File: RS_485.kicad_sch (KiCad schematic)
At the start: 17 parts, among them IC1 SP3071EEN-L/TR

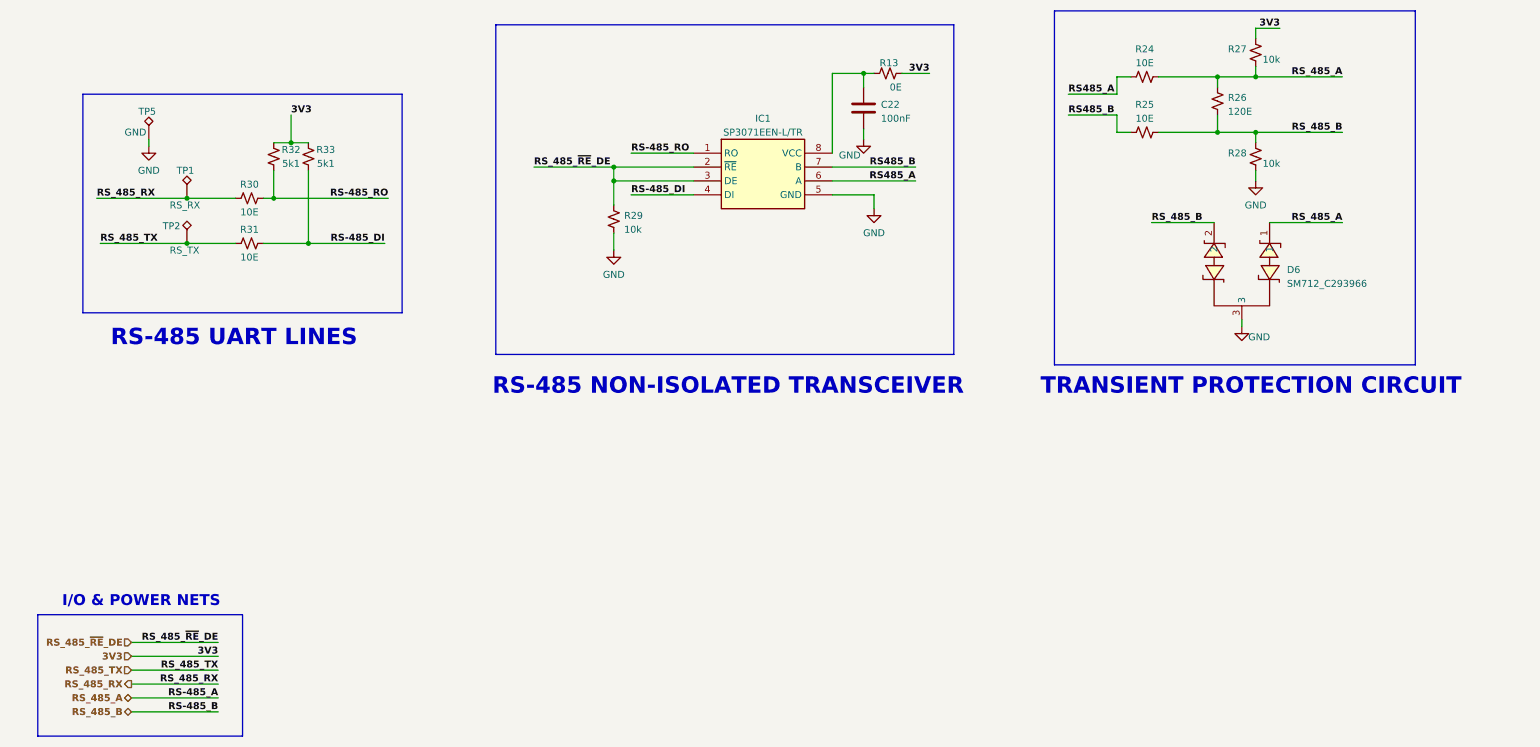
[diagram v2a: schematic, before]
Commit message: Arranged IP5306, Added support for USB-To-RS485
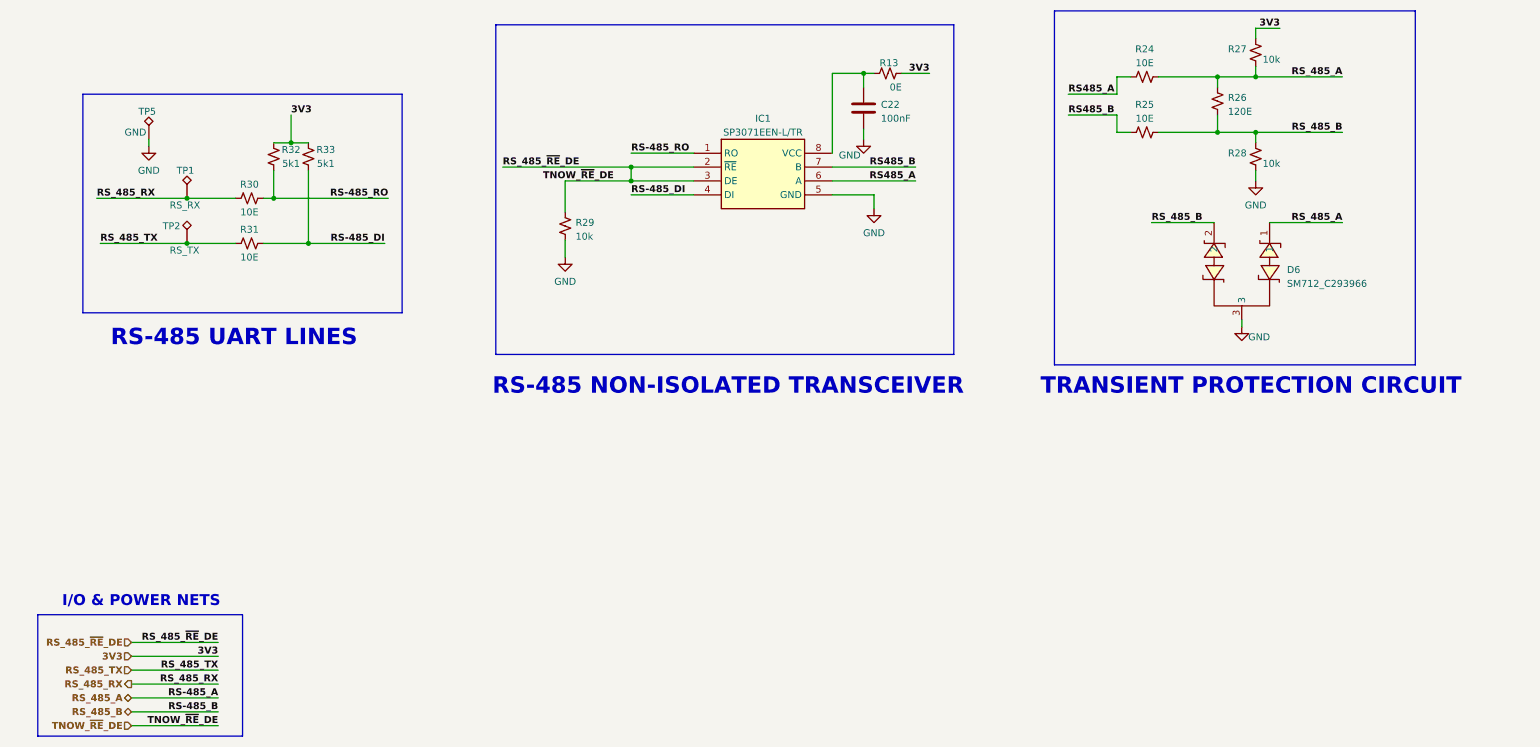
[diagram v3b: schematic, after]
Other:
- moved on the sheet: R29
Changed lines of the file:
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@@
   (junction (at 235.585 81.28) (diameter 0) (color 0 0 0 0)
   )
-  (junction (at 125.095 90.17) (diameter 0) (color 0 0 0 0)
+  (junction (at 128.27 87.63) (diameter 0) (color 0 0 0 0)
+  )
+  (junction (at 128.27 90.17) (diameter 0) (color 0 0 0 0)
   )
   (junction (at 46.99 101.6) (diameter 0) (color 0 0 0 0)
@@
   (junction (at 46.99 93.345) (diameter 0) (color 0 0 0 0)
   )
-  (junction (at 125.095 87.63) (diameter 0) (color 0 0 0 0)
-  )
   (junction (at 235.585 71.12) (diameter 0) (color 0 0 0 0)
   )
@@
     (stroke (width 0) (type default))
   )
-  (wire (pts (xy 125.095 94.615) (xy 125.095 90.17))
+  (wire (pts (xy 116.205 95.885) (xy 116.205 90.17))
     (stroke (width 0) (type default))
   )
@@
     (stroke (width 0) (type default))
   )
-  (wire (pts (xy 125.095 87.63) (xy 125.095 90.17))
+  (wire (pts (xy 128.27 87.63) (xy 128.27 90.17))
     (stroke (width 0) (type default))
   )
@@
     (stroke (width 1) (type default) (color 72 72 72 1))
   )
+  (wire (pts (xy 128.27 87.63) (xy 139.7 87.63))
+    (stroke (width 0) (type default))
+  )
   (wire (pts (xy 224.79 71.12) (xy 235.585 71.12))
     (stroke (width 0) (type default))
@@
     (stroke (width 0.5) (type default) (color 0 194 0 1))
   )
-  (wire (pts (xy 125.095 99.695) (xy 125.095 102.87))
-    (stroke (width 0) (type default))
-  )
   (wire (pts (xy 46.99 93.345) (xy 55.88 93.345))
     (stroke (width 0) (type default))
@@
     (stroke (width 0) (type default))
   )
+  (wire (pts (xy 104.775 87.63) (xy 128.27 87.63))
+    (stroke (width 0) (type default))
+  )
   (bus (pts (xy 103.505 61.595) (xy 103.505 121.92))
     (stroke (width 1) (type default) (color 72 72 72 1))
+  )
+  (wire (pts (xy 116.205 100.965) (xy 116.205 104.14))
+    (stroke (width 0) (type default))
+  )
+  (wire (pts (xy 52.705 189.865) (xy 36.83 189.865))
+    (stroke (width 0.5) (type default) (color 0 194 0 1))
   )
   (wire (pts (xy 62.865 88.265) (xy 62.865 93.345))
@@
     (stroke (width 1) (type default) (color 72 72 72 1))
   )
-  (wire (pts (xy 110.49 87.63) (xy 125.095 87.63))
-    (stroke (width 0) (type default))
-  )
-  (wire (pts (xy 125.095 90.17) (xy 139.7 90.17))
-    (stroke (width 0) (type default))
-  )
   (wire (pts (xy 240.03 116.84) (xy 240.03 115.57))
     (stroke (width 0) (type default))
@@
     (stroke (width 0.5) (type default) (color 255 0 0 1))
   )
-  (wire (pts (xy 125.095 87.63) (xy 139.7 87.63))
-    (stroke (width 0) (type default))
-  )
   (wire (pts (xy 128.27 85.09) (xy 139.7 85.09))
     (stroke (width 0) (type default))
@@
   )
   (wire (pts (xy 40.005 83.82) (xy 40.005 82.55))
+    (stroke (width 0) (type default))
+  )
+  (wire (pts (xy 128.27 90.17) (xy 116.205 90.17))
+    (stroke (width 0) (type default))
+  )
+  (wire (pts (xy 128.27 90.17) (xy 139.7 90.17))
     (stroke (width 0) (type default))
   )
@@
     (effects (font (size 1.27 1.27) (thickness 0.254) bold (color 0 0 0 1)) (justify right bottom))
   )
+  (label "TNOW_~{RE}_DE" (at 125.095 90.17 180) (fields_autoplaced)
+    (effects (font (size 1.27 1.27) bold (color 0 194 0 1)) (justify right bottom))
+  )
   (label "3V3" (at 182.88 70.485 180) (fields_autoplaced)
     (effects (font (size 1.27 1.27) (thickness 0.254) bold (color 255 0 0 1)) (justify right bottom))
@@
     (effects (font (size 1.27 1.27) (thickness 0.254) bold (color 0 0 255 1)) (justify right bottom))
   )
-  (label "RS_485_~{RE}_DE" (at 110.49 87.63 0) (fields_autoplaced)
+  (label "RS_485_~{RE}_DE" (at 104.775 87.63 0) (fields_autoplaced)
     (effects (font (size 1.27 1.27) bold (color 0 194 0 1)) (justify left bottom))
   )
@@
     (effects (font (size 1.27 1.27) (thickness 0.254) bold (color 0 0 255 1)) (justify left bottom))
   )
+  (label "TNOW_~{RE}_DE" (at 52.705 189.865 180) (fields_autoplaced)
+    (effects (font (size 1.27 1.27) bold (color 0 194 0 1)) (justify right bottom))
+  )
   (label "3V3" (at 247.015 62.23 180) (fields_autoplaced)
     (effects (font (size 1.27 1.27) (thickness 0.254) bold (color 255 0 0 1)) (justify right bottom))
@@
   (hierarchical_label "RS_485_B" (shape bidirectional) (at 36.83 187.325 180) (fields_autoplaced)
     (effects (font (size 1.27 1.27) bold (color 0 0 0 1)) (justify right))
+  )
+  (hierarchical_label "TNOW_~{RE}_DE" (shape input) (at 36.83 189.865 180) (fields_autoplaced)
+    (effects (font (size 1.27 1.27) bold (color 0 194 0 1)) (justify right))
   )
   (symbol (lib_id "ESP32-S3_DB:GND") (at 242.57 90.17 0) (unit 1)
@@
     )
   )
-  (symbol (lib_id "ESP32-S3_DB:GND") (at 125.095 102.87 0) (unit 1)
-    (in_bom yes) (on_board yes) (dnp no) (fields_autoplaced)
-    (property "Reference" "#PWR038" (at 125.095 109.22 0)
-      (effects (font (size 1.27 1.27)) hide)
-    )
-    (property "Value" "GND" (at 125.095 107.315 0)
-      (effects (font (size 1.27 1.27)))
-    )
-    (property "Footprint" "" (at 125.095 102.87 0)
-      (effects (font (size 1.27 1.27)) hide)
-    )
-    (property "Datasheet" "" (at 125.095 102.87 0)
+  (symbol (lib_id "ESP32-S3_DB:GND") (at 116.205 104.14 0) (unit 1)
+    (in_bom yes) (on_board yes) (dnp no) (fields_autoplaced)
+    (property "Reference" "#PWR038" (at 116.205 110.49 0)
+      (effects (font (size 1.27 1.27)) hide)
+    )
+    (property "Value" "GND" (at 116.205 108.585 0)
+      (effects (font (size 1.27 1.27)))
+    )
+    (property "Footprint" "" (at 116.205 104.14 0)
+      (effects (font (size 1.27 1.27)) hide)
+    )
+    (property "Datasheet" "" (at 116.205 104.14 0)
       (effects (font (size 1.27 1.27)) hide)
     )
@@
     )
   )
-  (symbol (lib_id "ESP32-S3_DB:R_Small_US") (at 125.095 97.155 180) (unit 1)
-    (in_bom yes) (on_board yes) (dnp no) (fields_autoplaced)
-    (property "Reference" "R29" (at 127 96.52 0)
+  (symbol (lib_id "ESP32-S3_DB:R_Small_US") (at 116.205 98.425 180) (unit 1)
+    (in_bom yes) (on_board yes) (dnp no) (fields_autoplaced)
+    (property "Reference" "R29" (at 118.11 97.79 0)
       (effects (font (size 1.27 1.27)) (justify right))
     )
-    (property "Value" "10k" (at 127 99.06 0)
+    (property "Value" "10k" (at 118.11 100.33 0)
       (effects (font (size 1.27 1.27)) (justify right))
     )
-    (property "Footprint" "ESP32-S3_Dev_Board:R_0402_1005Metric" (at 125.095 97.155 0)
-      (effects (font (size 1.27 1.27)) hide)
-    )
-    (property "Datasheet" "~" (at 125.095 97.155 0)
-      (effects (font (size 1.27 1.27)) hide)
-    )
-    (property "PN" "RC0402FR-0710KL" (at 125.095 97.155 0)
-      (effects (font (size 1.27 1.27)) hide)
-    )
+    (property "Footprint" "ESP32-S3_Dev_Board:R_0402_1005Metric" (at 116.205 98.425 0)
+      (effects (font (size 1.27 1.27)) hide)
+    )
+    (property "Datasheet" "~" (at 116.205 98.425 0)
+      (effects (font (size 1.27 1.27)) hide)
+    )
+    (property "PN" "RC0402FR-0710KL" (at 116.205 98.425 0)
+      (effects (font (size 1.27 1.27)) hide)
+    )

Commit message: First draft of component layout
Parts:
- removed IC1: SP3071EEN-L/TR, ESP32-S3_Dev_Board:SOP-8_3.9x4.9mm_P1.27mm, symbol ESP32-S3_DB:MAX485ESA+T
- added U6: SP3071EEN-L/TR, ESP32-S3_Dev_Board:SOP-8_3.9x4.9mm_P1.27mm, symbol ESP32-S3_DB:SP3071EEN-L/TR
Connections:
- net GND: now also U6.5 (GND)
- net RS-485_DI: now also U6.4 (DI)
- net RS-485_RO: now also U6.1 (RO)
- net RS485_A: now also U6.6 (A)
- net RS485_B: now also U6.7 (B)
- net RS_485_~{RE}_DE: now also U6.2 (~{RE}), U6.3 (DE)
- net at C22.1, R13.1: now also U6.8 (VCC)

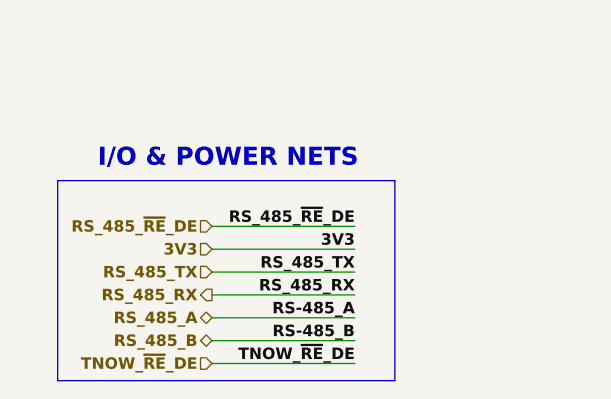
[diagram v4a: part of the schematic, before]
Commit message: Added selection jumper sheet and USB-UART option for board
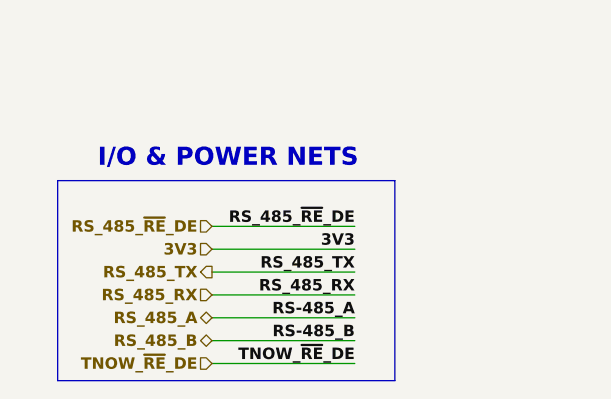
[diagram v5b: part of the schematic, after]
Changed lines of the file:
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@@
     (effects (font (size 1.27 1.27) (thickness 0.254) bold (color 0 0 0 1)) (justify left bottom))
   )
-  (hierarchical_label "RS_485_TX" (shape input) (at 36.83 179.705 180) (fields_autoplaced)
+  (hierarchical_label "RS_485_TX" (shape output) (at 36.83 179.705 180) (fields_autoplaced)
     (effects (font (size 1.27 1.27) bold (color 0 0 255 1)) (justify right))
   )
@@
     (effects (font (size 1.27 1.27) (thickness 0.254) bold (color 255 0 0 1)) (justify right))
   )
-  (hierarchical_label "RS_485_RX" (shape output) (at 36.83 182.245 180) (fields_autoplaced)
+  (hierarchical_label "RS_485_RX" (shape input) (at 36.83 182.245 180) (fields_autoplaced)
     (effects (font (size 1.27 1.27) bold (color 0 0 255 1)) (justify right))
   )

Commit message: Started ESP routing
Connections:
- net RS485_A renamed RS_485_P
- net RS485_B renamed RS_485_N
- net RS_485_A renamed RS485_P
- net RS_485_B renamed RS485_N
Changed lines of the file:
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@@
     (stroke (width 0) (type default))
   )
-  (bus (pts (xy 205.74 123.825) (xy 271.78 123.825))
-    (stroke (width 1) (type default) (color 72 72 72 1))
-  )
-  (wire (pts (xy 208.28 74.295) (xy 217.17 74.295))
+  (bus (pts (xy 201.295 123.825) (xy 271.78 123.825))
+    (stroke (width 1) (type default) (color 72 72 72 1))
+  )
+  (wire (pts (xy 206.375 74.295) (xy 217.17 74.295))
     (stroke (width 0) (type default))
   )
@@
     (stroke (width 0) (type default))
   )
-  (bus (pts (xy 271.78 59.055) (xy 205.74 59.055))
+  (bus (pts (xy 271.78 59.055) (xy 201.295 59.055))
     (stroke (width 1) (type default) (color 72 72 72 1))
   )
@@
     (stroke (width 0) (type default))
   )
-  (bus (pts (xy 205.74 59.055) (xy 205.74 123.825))
+  (bus (pts (xy 201.295 59.055) (xy 201.295 123.825))
     (stroke (width 1) (type default) (color 72 72 72 1))
   )
@@
     (stroke (width 0.5) (type default) (color 0 0 255 1))
   )
-  (wire (pts (xy 208.28 78.105) (xy 217.17 78.105))
+  (wire (pts (xy 206.375 78.105) (xy 217.17 78.105))
     (stroke (width 0) (type default))
   )
@@
     (effects (font (size 3 3) bold (color 255 0 0 1)) (justify left bottom))
   )
-  (label "RS_485_A" (at 258.445 97.79 180) (fields_autoplaced)
+  (label "RS485_P" (at 258.445 97.79 180) (fields_autoplaced)
     (effects (font (size 1.27 1.27) (thickness 0.254) bold (color 0 0 0 1)) (justify right bottom))
   )
@@
     (effects (font (size 1.27 1.27) (thickness 0.254) bold (color 255 0 0 1)) (justify right bottom))
   )
-  (label "RS-485_A" (at 52.705 184.785 180) (fields_autoplaced)
-    (effects (font (size 1.27 1.27) (thickness 0.254) bold (color 0 0 0 1)) (justify right bottom))
-  )
-  (label "RS_485_B" (at 258.445 81.28 180) (fields_autoplaced)
+  (label "RS485_P" (at 52.705 184.785 180) (fields_autoplaced)
+    (effects (font (size 1.27 1.27) (thickness 0.254) bold (color 0 0 0 1)) (justify right bottom))
+  )
+  (label "RS485_N" (at 258.445 81.28 180) (fields_autoplaced)
     (effects (font (size 1.27 1.27) (thickness 0.254) bold (color 0 0 0 1)) (justify right bottom))
   )
@@
     (effects (font (size 1.27 1.27) bold (color 0 194 0 1)) (justify left bottom))
   )
-  (label "RS485_B" (at 180.34 87.63 180) (fields_autoplaced)
+  (label "RS_485_N" (at 180.34 87.63 180) (fields_autoplaced)
     (effects (font (size 1.27 1.27) bold (color 0 0 255 1)) (justify right bottom))
   )
@@
     (effects (font (size 1.27 1.27) (thickness 0.254) bold (color 0 0 255 1)) (justify right bottom))
   )
-  (label "RS_485_A" (at 258.445 71.12 180) (fields_autoplaced)
+  (label "RS485_P" (at 258.445 71.12 180) (fields_autoplaced)
     (effects (font (size 1.27 1.27) (thickness 0.254) bold (color 0 0 0 1)) (justify right bottom))
   )
@@
     (effects (font (size 1.27 1.27) bold (color 0 0 255 1)) (justify left bottom))
   )
-  (label "RS-485_B" (at 52.705 187.325 180) (fields_autoplaced)
-    (effects (font (size 1.27 1.27) (thickness 0.254) bold (color 0 0 0 1)) (justify right bottom))
-  )
-  (label "RS485_A" (at 208.28 74.295 0) (fields_autoplaced)
+  (label "RS485_N" (at 52.705 187.325 180) (fields_autoplaced)
+    (effects (font (size 1.27 1.27) (thickness 0.254) bold (color 0 0 0 1)) (justify right bottom))
+  )
+  (label "RS_485_P" (at 206.375 74.295 0) (fields_autoplaced)
     (effects (font (size 1.27 1.27) bold (color 0 0 255 1)) (justify left bottom))
   )
@@
     (effects (font (size 1.27 1.27) bold (color 0 0 255 1)) (justify left bottom))
   )
-  (label "RS485_B" (at 208.28 78.105 0) (fields_autoplaced)
+  (label "RS_485_N" (at 206.375 78.105 0) (fields_autoplaced)
     (effects (font (size 1.27 1.27) bold (color 0 0 255 1)) (justify left bottom))
   )
@@
     (effects (font (size 1.27 1.27) bold (color 0 194 0 1)) (justify right bottom))
   )
-  (label "RS485_A" (at 180.34 90.17 180) (fields_autoplaced)
-    (effects (font (size 1.27 1.27) bold (color 0 0 255 1)) (justify right bottom))
-  )
-  (label "RS_485_B" (at 223.52 97.79 0) (fields_autoplaced)
+  (label "RS_485_P" (at 180.34 90.17 180) (fields_autoplaced)
+    (effects (font (size 1.27 1.27) bold (color 0 0 255 1)) (justify right bottom))
+  )
+  (label "RS485_N" (at 223.52 97.79 0) (fields_autoplaced)
     (effects (font (size 1.27 1.27) (thickness 0.254) bold (color 0 0 0 1)) (justify left bottom))
   )
@@
     (effects (font (size 1.27 1.27) bold (color 0 0 255 1)) (justify right))
   )
-  (hierarchical_label "RS_485_A" (shape bidirectional) (at 36.83 184.785 180) (fields_autoplaced)
+  (hierarchical_label "RS485_P" (shape bidirectional) (at 36.83 184.785 180) (fields_autoplaced)
     (effects (font (size 1.27 1.27) bold (color 0 0 0 1)) (justify right))
   )
@@
     (effects (font (size 1.27 1.27) bold (color 0 194 0 1)) (justify right))
   )
-  (hierarchical_label "RS_485_B" (shape bidirectional) (at 36.83 187.325 180) (fields_autoplaced)
+  (hierarchical_label "RS485_N" (shape bidirectional) (at 36.83 187.325 180) (fields_autoplaced)
     (effects (font (size 1.27 1.27) bold (color 0 0 0 1)) (justify right))
   )
